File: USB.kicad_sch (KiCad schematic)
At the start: 2 parts, among them P1 USB_C_Plug_USB2.0

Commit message: Add files via upload
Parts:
- removed P1: USB_C_Plug_USB2.0, symbol Connector:USB_C_Plug_USB2.0
- added C10, C11, C13, C14, C15, C18, C19: 0.1uF, symbol Device:C
- added C12, C16: 1uF, symbol Device:C
- added C17: 10uF, symbol Device:C_Polarized_US
- added C20, C21: C, symbol Device:C
- added C22, C24, C25, C26: 100uF/10V, symbol Device:C_Polarized_US
- added C23, C27, C28, C29: 0.1uF/10V, symbol Device:C
- added D3: LED, symbol Device:LED
- added J1, J2, J3, J4, J5: USB_A, symbol Connector:USB_A
- added L1, L2, L3, L4, L5, L6: L, symbol Device:L
- added R10, R6: 10k, symbol Device:R
- added R11: 20k, symbol Device:R
- added R5: 680, symbol Device:R
- added R7: 47k, symbol Device:R
- added R8: 100k, symbol Device:R
- added R9: 470, symbol Device:R
- added TH1, TH2, TH3, TH4: 500mA/6V, symbol Device:Thermistor_PTC
- added U4, U5, U6: SRV05-4, Package_TO_SOT_SMD:SOT-23-6, symbol Power_Protection:SRV05-4
- added Y1: 12MHz, symbol Device:Crystal
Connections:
- net AVDD: now reaches U3.1 (AVDD)
- net AVDD: now also U3.10 (AVDD), U3.5 (AVDD), C10.2, C11.1, C12.1, C13.2, C18.1, L1.2
- net DM4: now reaches U3.11 (DM4)
- net DM4: now also J5.2 (D-), U6.1 (IO1)
- net DP4: now reaches U3.12 (DP4)
- net DP4: now also J5.3 (D+), U6.3 (IO2)
- net RESET: now reaches U3.13 (RESET)
- net RESET: now also C19.1, R6.2, R7.1
- net GND: now reaches U3.15 (GND)
- net GND: now also C10.1, C11.2, C12.2, C13.1, C14.2, C15.2, C16.2, C17.2, C18.2, C19.2, C20.2, C21.2, C22.2, C23.2, C24.2, C25.2, C26.2, C27.2, C28.2, C29.2, J1.4 (GND), J1.5 (Shield), J2.4 (GND), J2.5 (Shield), J3.4 (GND), J3.5 (Shield), J4.4 (GND), J4.5 (Shield), J5.4 (GND), J5.5 (Shield), R11.2, R5.1, R7.2, U4.5 (VP), U5.5 (VP), U6.5 (VP)
- net DVDD: now reaches U3.16 (DVDD)
- net DVDD: now also U3.24 (V33), C14.1, C17.1, L1.1, R8.1, R9.1
- net PGANG: now reaches U3.18 (PGANG)
- net PGANG: now also D3.1 (K), R8.2
- net DM2: now reaches U3.2 (DM2)
- net DM2: now also J3.2 (D-), U5.1 (IO1)
- net OVERCUR1: now reaches U3.21 (OVCUR1)
- net OVERCUR1: now also R10.2, R11.1
- net +5V: now reaches U3.23 (V5)
- net +5V: now also C15.1, C16.1, L2.2, R10.1, R6.1, TH1.2, TH2.2, TH3.2, TH4.2, U4.2 (VN), U5.2 (VN), U6.2 (VN)
- net DM0: now reaches U3.25 (DM0)
- net DM0: now also J1.2 (D-), U4.3 (IO2)
- net DP0: now reaches U3.26 (DP0)
- net DP0: now also J1.3 (D+), U4.1 (IO1)
- net DM1: now reaches U3.27 (DM1)
- net DM1: now also J2.2 (D-), U5.4 (IO3)
- net DP1: now reaches U3.28 (DP1)
- net DP1: now also J2.3 (D+), U5.6 (IO4)
- net DP2: now reaches U3.3 (DP2)
- net DP2: now also J3.3 (D+), U5.3 (IO2)
- net at U3.4 (RREF): now also R5.2
- net X1: now reaches U3.6 (X1)
- net X1: now also C20.1, Y1.1
- net X2: now reaches U3.7 (X2)
- net X2: now also C21.1, Y1.2
- net DM3: now reaches U3.8 (DM3)
- net DM3: now also J4.2 (D-), U6.4 (IO3)
- net DP3: now reaches U3.9 (DP3)
- net DP3: now also J4.3 (D+), U6.6 (IO4)
- new net: C27.1, J3.1 (VBUS), L4.1
- new net: C26.1, L4.2, TH2.1
- new net: C23.1, J2.1 (VBUS), L3.1
- new net: C24.1, L5.2, TH4.1
- new net: C22.1, L3.2, TH1.1
- new net: C29.1, J4.1 (VBUS), L5.1
- new net: J1.1 (VBUS), L2.1
- new net: D3.2 (A), R9.2
- new net: C25.1, L6.2, TH3.1
- new net: C28.1, J5.1 (VBUS), L6.1
- no-connect marks 0 -> 7
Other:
- note added: "Alle Spulen müssen noch definiert werden"
- note added: "C20 & C21 werden nach dem Datenblatt von Y1 bestimmt"
- note added: "Down-Stream"
- note added: "Gang indicator"
- note added: "OSC"
- note added: "Overcurrent"
- note added: "Reset"
- note added: "USB-Hub IC"
- note added: "Up-Stream"
- moved on the sheet: U3

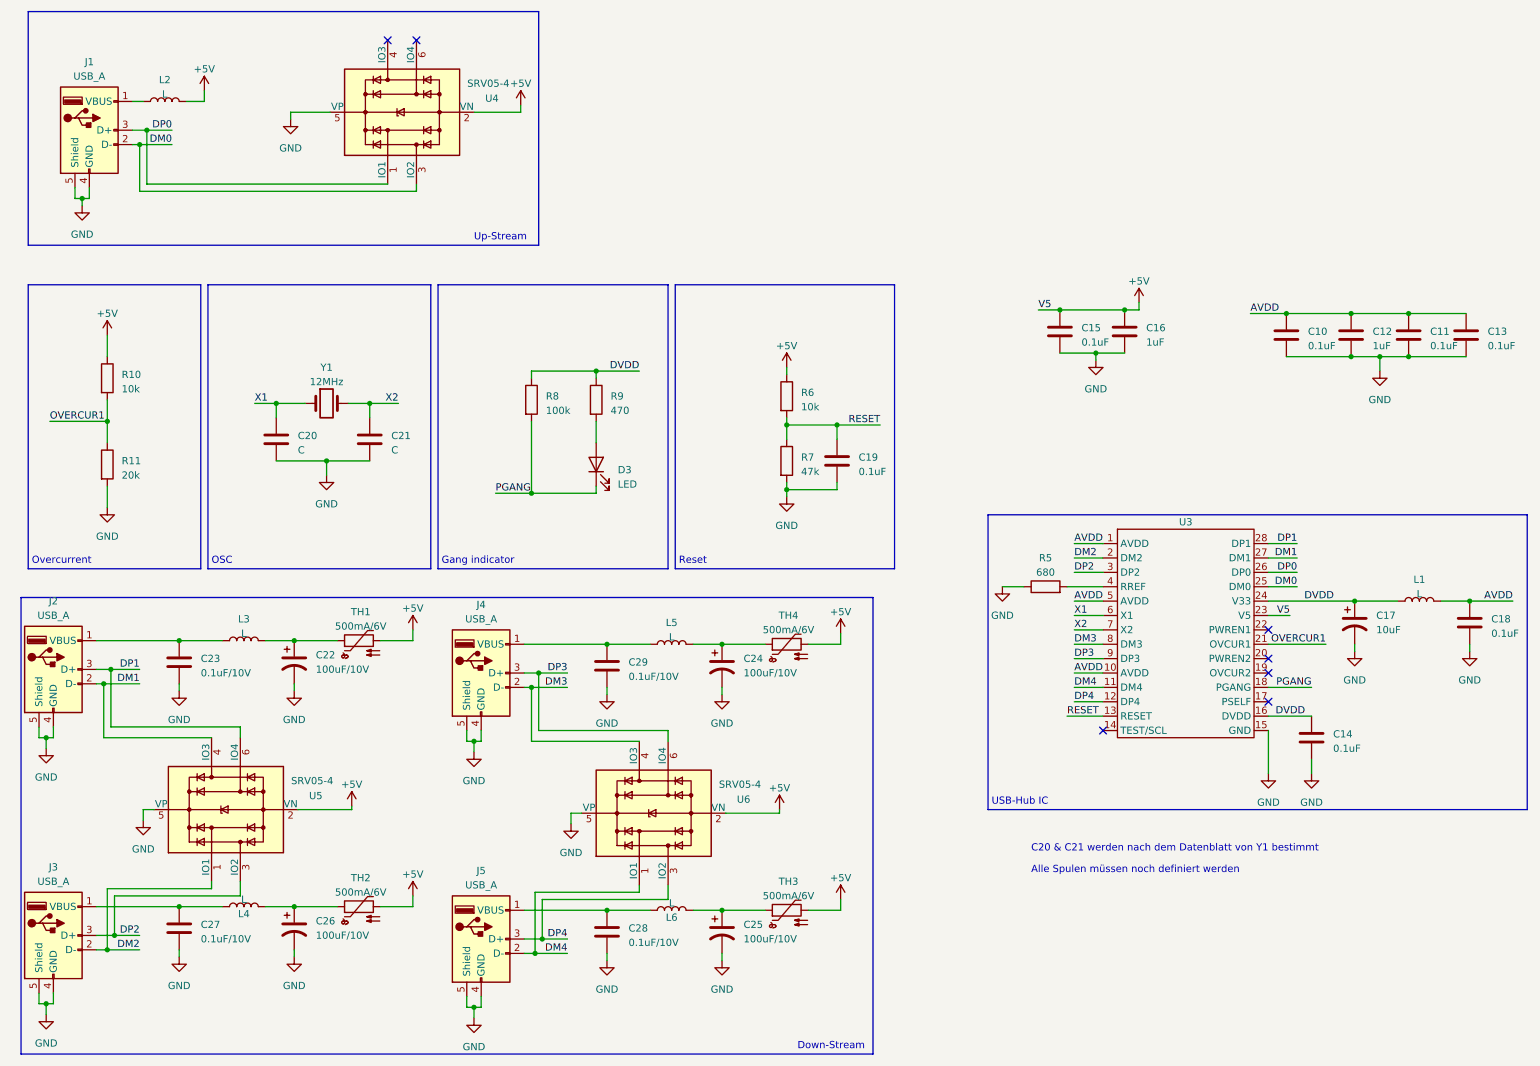
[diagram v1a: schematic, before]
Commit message: Schematic fertig und Layout gerouted
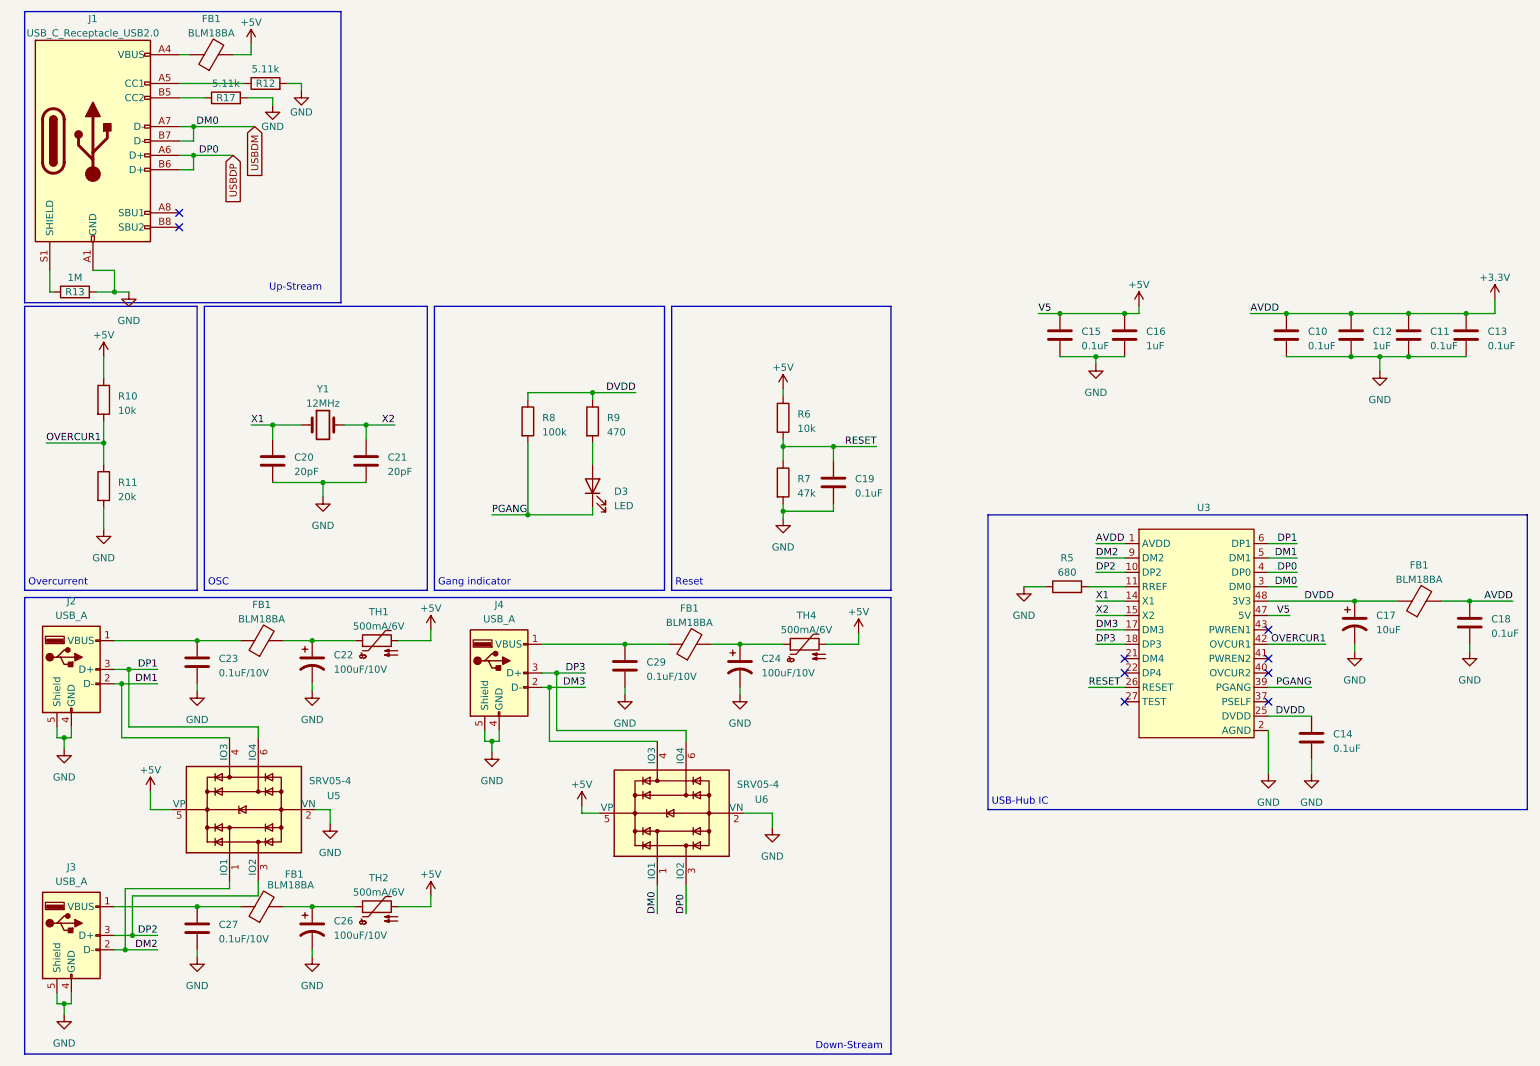
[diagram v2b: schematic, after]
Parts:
- removed C25: 100uF/10V, symbol Device:C_Polarized_US
- removed C28: 0.1uF/10V, symbol Device:C
- removed J1, J5: USB_A, symbol Connector:USB_A
- removed L1, L2, L3, L4, L5, L6: L, symbol Device:L
- removed TH3: 500mA/6V, symbol Device:Thermistor_PTC
- removed U4: SRV05-4, Package_TO_SOT_SMD:SOT-23-6, symbol Power_Protection:SRV05-4
- added FB1 (x5): BLM18BA, Inductor_SMD:L_0603_1608Metric_Pad1.05x0.95mm_HandSolder, symbol Device:FerriteBead
- added J1: USB_C_Receptacle_USB2.0, Connector_USB:USB_C_Receptacle_GCT_USB4085, symbol Connector:USB_C_Receptacle_USB2.0
- added R12, R17: 5.11k, Resistor_SMD:R_1206_3216Metric_Pad1.30x1.75mm_HandSolder, symbol Device:R
- added R13: 1M, Resistor_SMD:R_1206_3216Metric_Pad1.30x1.75mm_HandSolder, symbol Device:R
- C10, C11, C13, C14, C15, C18, C19, C23, C27, C29: footprint (none) -> Capacitor_SMD:C_0805_2012Metric_Pad1.18x1.45mm_HandSolder
- C12, C16: footprint (none) -> Capacitor_SMD:CP_Elec_4x5.4
- C17: footprint (none) -> Capacitor_SMD:CP_Elec_4x5.8
- C20, C21: value C -> 20pF; footprint (none) -> Capacitor_SMD:C_0805_2012Metric_Pad1.18x1.45mm_HandSolder
- C22, C24, C26: footprint (none) -> Capacitor_SMD:CP_Elec_6.3x7.7
- D3: footprint (none) -> LED_SMD:LED_0805_2012Metric_Pad1.15x1.40mm_HandSolder
- J2, J3, J4: footprint (none) -> Connector_USB:USB_A_TE_292303-7_Horizontal
- R10, R11, R5, R6, R7, R8, R9: footprint (none) -> Resistor_SMD:R_1206_3216Metric_Pad1.30x1.75mm_HandSolder
- TH1, TH2, TH4: footprint (none) -> Fuse:Fuse_0805_2012Metric_Pad1.15x1.40mm_HandSolder
- U3: footprint (none) -> Package_QFP:LQFP-48_7x7mm_P0.5mm
- Y1: footprint (none) -> Crystal:Crystal_SMD_ECS_CSM3X-2Pin_7.6x4.1mm
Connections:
- net DM0 is gone; now on net DVDD: U3.25 (DVDD)
- net DP0 is gone; now on net RESET: U3.26 (RESET)
- net +5V: now also U3.47 (5V), U5.5 (VP), U6.5 (VP), FB1.2; no longer U3.23 (V5), U5.2 (VN), U6.2 (VN)
- net DM1: now also U3.5 (DM1); no longer U3.27 (DM1)
- net DM2: now also U3.9 (DM2); no longer U3.2 (DM2)
- net DM3: now also U3.17 (DM3); no longer U3.8 (DM3)
- net DP1: now also U3.6 (DP1); no longer U3.28 (DP1)
- net DP2: now also U3.10 (DP2); no longer U3.3 (DP2)
- net DP3: now also U3.18 (DP3); no longer U3.9 (DP3)
- net DVDD: now also U3.34 (DVDD), U3.38 (DVDD), U3.44 (DVDD), U3.48 (3V3), FB1.1; no longer U3.16 (DVDD), U3.24 (V33)
- net OVERCUR1: now also U3.42 (OVCUR1); no longer U3.21 (OVCUR1)
- net PGANG: now also U3.39 (PGANG); no longer U3.18 (PGANG)
- net RESET: no longer U3.13 (RESET)
- net X1: now also U3.14 (X1); no longer U3.6 (X1)
- net X2: now also U3.15 (X2); no longer U3.7 (X2)
- net at C27.1, J3.1 (VBUS): now also FB1.1
- net at C26.1, TH2.1: now also FB1.2
- net at C23.1, J2.1 (VBUS): now also FB1.1
- net at C24.1, TH4.1: now also FB1.2
- net at C22.1, TH1.1: now also FB1.2
- net +3.3V: now reaches U3.19 (AVDD)
- net +3.3V: now also C10.2, C11.1, C12.1, C13.2, C18.1, U3.1 (AVDD), U3.12 (AVDD), U3.16 (AVDD), U3.7 (AVDD), FB1.2
- net AGND: now reaches U3.20 (AGND)
- net AGND: now also C10.1, C11.2, C12.2, C13.1, C14.2, C15.2, C16.2, C17.2, C18.2, C19.2, C20.2, C21.2, C22.2, C23.2, C24.2, C26.2, C27.2, C29.2, J2.4 (GND), J2.5 (Shield), J3.4 (GND), J3.5 (Shield), J4.4 (GND), J4.5 (Shield), R11.2, R5.1, R7.2, U3.13 (AGND), U3.2 (AGND), U3.8 (AGND), U5.2 (VN), U6.2 (VN), J1.A1 (GND), J1.A12 (GND), J1.B1 (GND), J1.B12 (GND), R12.2, R13.2, R17.2
- net at R5.2: now also U3.11 (RREF); no longer U3.4 (RREF)
- net at C29.1, J4.1 (VBUS): now also FB1.1
- removed net AVDD: C10.2, C11.1, C12.1, C13.2, C18.1, U3.1 (AVDD), U3.10 (AVDD), U3.5 (AVDD)
- net DM4 renamed USBDM
- net USBDM: now also U3.3 (DM0), J1.A7 (D-), J1.B7 (D-); no longer U3.11 (DM4)
- net DP4 renamed USBDP
- net USBDP: now also U3.4 (DP0), J1.A6 (D+), J1.B6 (D+); no longer U3.12 (DP4)
- removed net GND: C10.1, C11.2, C12.2, C13.1, C14.2, C15.2, C16.2, C17.2, C18.2, C19.2, C20.2, C21.2, C22.2, C23.2, C24.2, C26.2, C27.2, C29.2, J2.4 (GND), J2.5 (Shield), J3.4 (GND), J3.5 (Shield), J4.4 (GND), J4.5 (Shield), R11.2, R5.1, R7.2, U3.15 (GND), U5.5 (VP), U6.5 (VP)
- new net: FB1.1, J1.A4 (VBUS), J1.A9 (VBUS), J1.B4 (VBUS), J1.B9 (VBUS)
- new net: J1.B5 (CC2), R17.1
- new net: J1.A5 (CC1), R12.1
- new net: J1.S1 (SHIELD), R13.1
- no-connect marks 7 -> 9
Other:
- note removed: "Alle Spulen müssen noch definiert werden"
- note removed: "C20 & C21 werden nach dem Datenblatt von Y1 bestimmt"
- moved on the sheet: C15, C16, C19, C20, C21, C22, C23, C24, C26, C27, C29, D3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

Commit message: Neue Anordnung für bessere Usb Leitungen
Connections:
- net DM1 renamed D_N1
- net DM2 renamed D_N2
- net DM3 renamed D_N3
- net DP1 renamed D_P1
- net DP2 renamed D_P2
- net DP3 renamed D_P3
- net USBDM renamed USBD_N
- net USBDP renamed USBD_P
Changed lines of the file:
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@@
     (effects (font (size 1.27 1.27)) (justify left bottom))
   )
-  (label "DP3" (at 201.93 124.46 0) (fields_autoplaced)
+  (label "D_P3" (at 201.93 124.46 0) (fields_autoplaced)
     (effects (font (size 1.27 1.27)) (justify left bottom))
   )
-  (label "DM0" (at 124.46 172.085 90) (fields_autoplaced)
+  (label "D_N0" (at 124.46 172.085 90) (fields_autoplaced)
     (effects (font (size 1.27 1.27)) (justify left bottom))
   )
-  (label "DP2" (at 36.195 175.895 180) (fields_autoplaced)
+  (label "D_P2" (at 36.195 175.895 180) (fields_autoplaced)
     (effects (font (size 1.27 1.27)) (justify right bottom))
   )
@@
     (effects (font (size 1.27 1.27)) (justify left bottom))
   )
-  (label "DM3" (at 111.76 132.08 180) (fields_autoplaced)
+  (label "D_N3" (at 111.76 132.08 180) (fields_autoplaced)
     (effects (font (size 1.27 1.27)) (justify right bottom))
   )
-  (label "DM1" (at 237.49 109.22 180) (fields_autoplaced)
+  (label "D_N1" (at 237.49 109.22 180) (fields_autoplaced)
     (effects (font (size 1.27 1.27)) (justify right bottom))
   )
@@
     (effects (font (size 1.27 1.27)) (justify left bottom))
   )
-  (label "DM0" (at 46.99 33.02 180) (fields_autoplaced)
+  (label "D_N0" (at 46.99 33.02 180) (fields_autoplaced)
     (effects (font (size 1.27 1.27)) (justify right bottom))
   )
-  (label "DP0" (at 46.99 38.1 180) (fields_autoplaced)
+  (label "D_P0" (at 46.99 38.1 180) (fields_autoplaced)
     (effects (font (size 1.27 1.27)) (justify right bottom))
   )
@@
     (effects (font (size 1.27 1.27)) (justify right bottom))
   )
-  (label "DM2" (at 201.93 109.22 0) (fields_autoplaced)
+  (label "D_N2" (at 201.93 109.22 0) (fields_autoplaced)
     (effects (font (size 1.27 1.27)) (justify left bottom))
   )
-  (label "DP1" (at 237.49 106.68 180) (fields_autoplaced)
+  (label "D_P1" (at 237.49 106.68 180) (fields_autoplaced)
     (effects (font (size 1.27 1.27)) (justify right bottom))
   )
-  (label "DM3" (at 201.93 121.92 0) (fields_autoplaced)
+  (label "D_N3" (at 201.93 121.92 0) (fields_autoplaced)
     (effects (font (size 1.27 1.27)) (justify left bottom))
   )
-  (label "DP3" (at 111.76 129.54 180) (fields_autoplaced)
+  (label "D_P3" (at 111.76 129.54 180) (fields_autoplaced)
     (effects (font (size 1.27 1.27)) (justify right bottom))
   )
@@
     (effects (font (size 1.27 1.27)) (justify right bottom))
   )
-  (label "DP2" (at 201.93 111.76 0) (fields_autoplaced)
+  (label "D_P2" (at 201.93 111.76 0) (fields_autoplaced)
     (effects (font (size 1.27 1.27)) (justify left bottom))
   )
-  (label "DM1" (at 36.195 131.445 180) (fields_autoplaced)
+  (label "D_N1" (at 36.195 131.445 180) (fields_autoplaced)
     (effects (font (size 1.27 1.27)) (justify right bottom))
   )
@@
     (effects (font (size 1.27 1.27)) (justify left bottom))
   )
-  (label "DM0" (at 237.49 114.3 180) (fields_autoplaced)
+  (label "D_N0" (at 237.49 114.3 180) (fields_autoplaced)
     (effects (font (size 1.27 1.27)) (justify right bottom))
   )
@@
     (effects (font (size 1.27 1.27)) (justify left bottom))
   )
-  (label "DM2" (at 36.195 178.435 180) (fields_autoplaced)
+  (label "D_N2" (at 36.195 178.435 180) (fields_autoplaced)
     (effects (font (size 1.27 1.27)) (justify right bottom))
   )
@@
     (effects (font (size 1.27 1.27)) (justify left bottom))
   )
-  (label "DP0" (at 129.54 172.085 90) (fields_autoplaced)
+  (label "D_P0" (at 129.54 172.085 90) (fields_autoplaced)
     (effects (font (size 1.27 1.27)) (justify left bottom))
   )
-  (label "DP0" (at 237.49 111.76 180) (fields_autoplaced)
+  (label "D_P0" (at 237.49 111.76 180) (fields_autoplaced)
     (effects (font (size 1.27 1.27)) (justify right bottom))
   )
@@
     (effects (font (size 1.27 1.27)) (justify left bottom))
   )
-  (label "DP1" (at 36.195 128.905 180) (fields_autoplaced)
+  (label "D_P1" (at 36.195 128.905 180) (fields_autoplaced)
     (effects (font (size 1.27 1.27)) (justify right bottom))
   )
-  (global_label "USBDM" (shape input) (at 53.34 33.02 270) (fields_autoplaced)
+  (global_label "USBD_N" (shape input) (at 53.34 33.02 270) (fields_autoplaced)
     (effects (font (size 1.27 1.27)) (justify right))
-    (property "Intersheetrefs" "${INTERSHEET_REFS}" (at 53.34 42.4572 90)
+    (property "Intersheetrefs" "${INTERSHEET_REFS}" (at 53.34 43.3039 90)
       (effects (font (size 1.27 1.27)) (justify right) hide)
     )
   )
-  (global_label "USBDP" (shape input) (at 49.53 38.1 270) (fields_autoplaced)
+  (global_label "USBD_P" (shape input) (at 49.53 38.1 270) (fields_autoplaced)
     (effects (font (size 1.27 1.27)) (justify right))
-    (property "Intersheetrefs" "${INTERSHEET_REFS}" (at 49.53 47.3558 90)
+    (property "Intersheetrefs" "${INTERSHEET_REFS}" (at 49.53 48.3234 90)
       (effects (font (size 1.27 1.27)) (justify right) hide)
     )
